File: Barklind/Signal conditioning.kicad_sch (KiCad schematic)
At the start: 37 parts, among them J1 Conn_01x07_Socket, J10 Conn_01x04_Pin, J11 Conn_01x04_Pin, J12 Conn_01x04_Pin, J13 Conn_01x04_Pin, J14 Conn_01x04_Pin, J15 Conn_01x03_Pin, J16 Conn_01x03_Pin, J17 Conn_01x03_Pin, J18 Conn_01x03_Pin, J19 Conn_01x03_Pin, J2 Conn_01x06_Socket, J20 Conn_01x03_Pin, J21 Conn_01x03_Socket, J22 Conn_01x03_Socket, J23 Conn_01x03_Socket, J24 Conn_01x03_Socket, J25 Conn_01x03_Socket, J26 Conn_01x03_Socket, J3 Conn_01x02_Socket, J4 Conn_01x03_Socket, J5 Conn_01x07_Pin, J6 Conn_01x06_Pin, J7 Conn_01x02_Pin, J8 Conn_01x03_Pin, J9 Conn_01x04_Pin, U7 74HCT04

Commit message: Restructured project, Changed kibot configurations into different files Changed github actions for the different jobs
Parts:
- J7: footprint TerminalBlock_Phoenix:TerminalBlock_Phoenix_PT-1,5-2-3.5-H_1x02_P3.50mm_Horizontal -> TerminalBlock_Phoenix:TerminalBlock_Phoenix_MKDS-3-2-5.08_1x02_P5.08mm_Horizontal
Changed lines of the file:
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@@
 			)
 		)
-		(property "Footprint" "TerminalBlock_Phoenix:TerminalBlock_Phoenix_PT-1,5-2-3.5-H_1x02_P3.50mm_Horizontal"
+		(property "Footprint" "TerminalBlock_Phoenix:TerminalBlock_Phoenix_MKDS-3-2-5.08_1x02_P5.08mm_Horizontal"
 			(at 86.36 157.48 0)
 			(effects

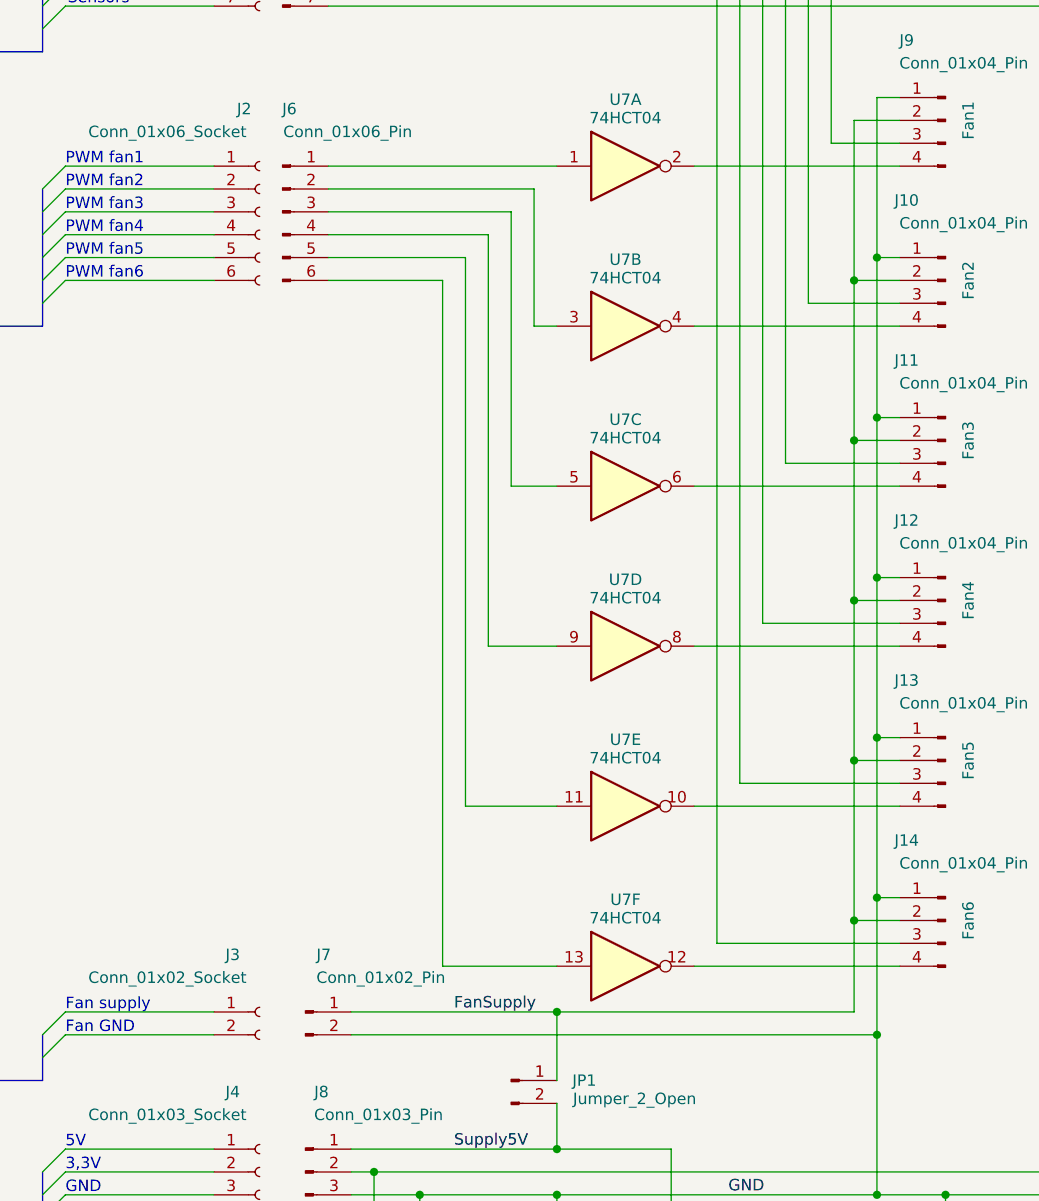
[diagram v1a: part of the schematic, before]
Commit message: Added pin header for pulling down unused inverter inputs
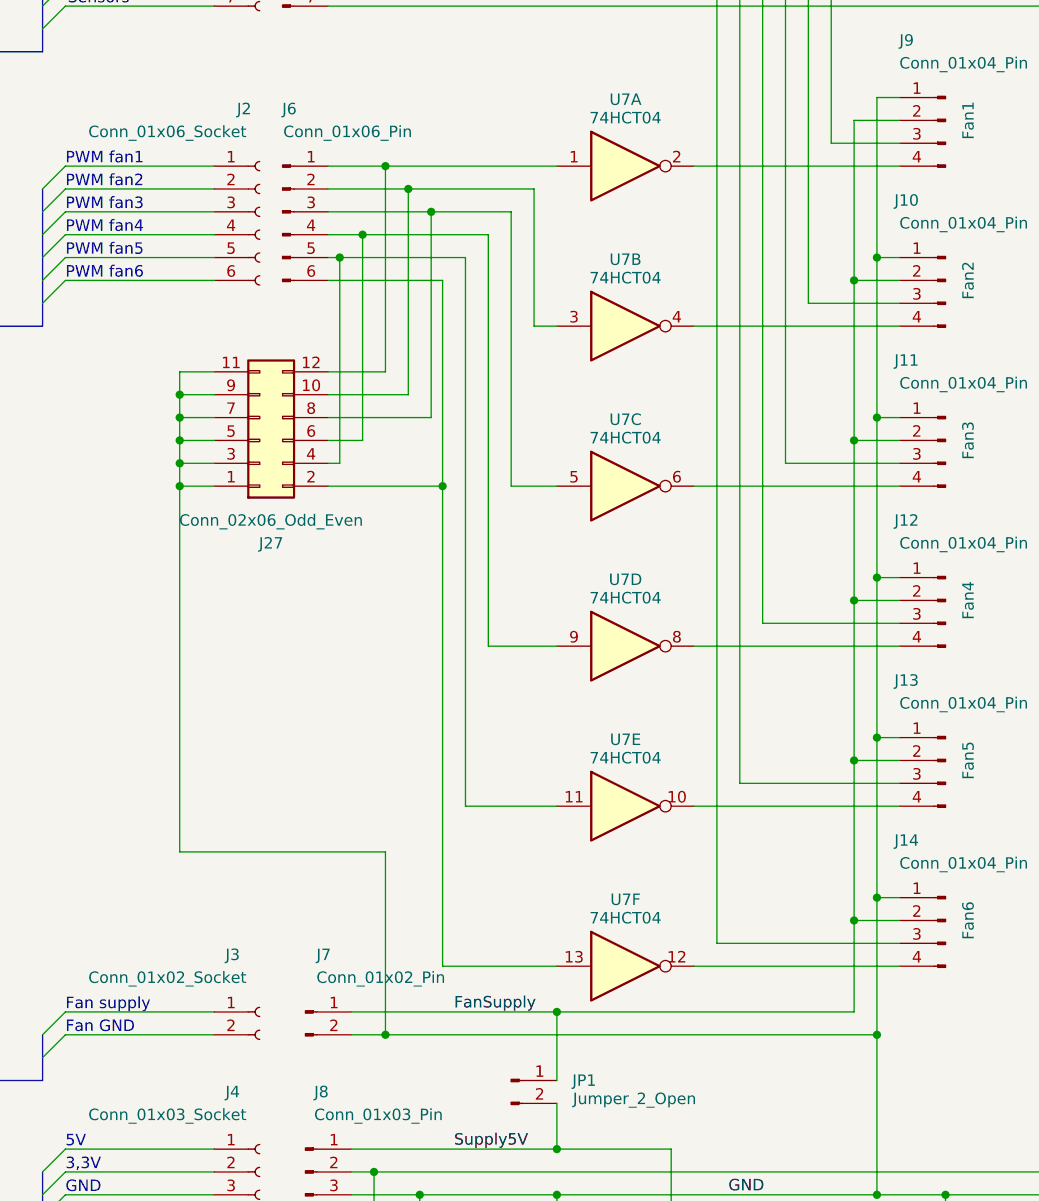
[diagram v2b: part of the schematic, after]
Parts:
- added J27: Conn_02x06_Odd_Even, Connector_PinHeader_1.27mm:PinHeader_2x06_P1.27mm_Vertical, symbol Connector_Generic:Conn_02x06_Odd_Even
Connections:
- net GND: now also J27.1 (Pin_1), J27.11 (Pin_11), J27.3 (Pin_3), J27.5 (Pin_5), J27.7 (Pin_7), J27.9 (Pin_9)
- net at J6.6 (Pin_6), U7.13: now also J27.2 (Pin_2)
- net at J6.2 (Pin_2), U7.3: now also J27.10 (Pin_10)
- net at J6.3 (Pin_3), U7.5: now also J27.8 (Pin_8)
- net at J6.5 (Pin_5), U7.11: now also J27.4 (Pin_4)
- net at J6.4 (Pin_4), U7.9: now also J27.6 (Pin_6)
- net at J6.1 (Pin_1), U7.1: now also J27.12 (Pin_12)

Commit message: Changed PCB to 4 layer and created manufacture files
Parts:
- J10, J11, J12, J13, J14, J9: footprint Connector_Molex:Molex_KK-254_AE-6410-04A_1x04_P2.54mm_Vertical -> Connector:FanPinHeader_1x04_P2.54mm_Vertical
- J7: footprint TerminalBlock_Phoenix:TerminalBlock_Phoenix_MKDS-3-2-5.08_1x02_P5.08mm_Horizontal -> Phoenix:PHOENIX_1705469
- R7: footprint Resistor_SMD:R_2010_5025Metric_Pad1.40x2.65mm_HandSolder -> Resistor_SMD:R_1206_3216Metric_Pad1.30x1.75mm_HandSolder
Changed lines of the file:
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@@
 	(label "GND"
 		(at 133.35 177.8 0)
+		(fields_autoplaced yes)
 		(effects
 			(font
@@
 	(label "FanSupply"
 		(at 102.87 157.48 0)
+		(fields_autoplaced yes)
 		(effects
 			(font
@@
 	(label "Supply5V"
 		(at 102.87 172.72 0)
+		(fields_autoplaced yes)
 		(effects
 			(font
@@
 		(shape output)
 		(at 228.6 119.38 0)
+		(fields_autoplaced yes)
 		(effects
 			(font
@@
 		(shape output)
 		(at 228.6 101.6 0)
+		(fields_autoplaced yes)
 		(effects
 			(font
@@
 		(shape input)
 		(at 50.8 50.8 180)
+		(fields_autoplaced yes)
 		(effects
 			(font
@@
 		(shape output)
 		(at 228.6 66.04 0)
+		(fields_autoplaced yes)
 		(effects
 			(font
@@
 		(shape output)
 		(at 228.6 137.16 0)
+		(fields_autoplaced yes)
 		(effects
 			(font
@@
 		(shape output)
 		(at 228.6 154.94 0)
+		(fields_autoplaced yes)
 		(effects
 			(font
@@
 		(shape input)
 		(at 50.8 182.88 180)
+		(fields_autoplaced yes)
 		(effects
 			(font
@@
 		(shape output)
 		(at 228.6 83.82 0)
+		(fields_autoplaced yes)
 		(effects
 			(font
@@
 		(shape output)
 		(at 50.8 81.28 180)
+		(fields_autoplaced yes)
 		(effects
 			(font
@@
 		(shape input)
 		(at 50.8 165.1 180)
+		(fields_autoplaced yes)
 		(effects
 			(font
@@
 			)
 		)
-		(property "Footprint" "Connector_Molex:Molex_KK-254_AE-6410-04A_1x04_P2.54mm_Vertical"
+		(property "Footprint" "Connector:FanPinHeader_1x04_P2.54mm_Vertical"
 			(at 157.48 147.32 0)
 			(effects
@@
 			)
 		)
-		(property "Footprint" "Connector_Molex:Molex_KK-254_AE-6410-04A_1x04_P2.54mm_Vertical"
+		(property "Footprint" "Connector:FanPinHeader_1x04_P2.54mm_Vertical"
 			(at 157.48 76.2 0)
 			(effects
@@
 			)
 		)
-		(property "Footprint" "Resistor_SMD:R_2010_5025Metric_Pad1.40x2.65mm_HandSolder"
+		(property "Footprint" "Resistor_SMD:R_1206_3216Metric_Pad1.30x1.75mm_HandSolder"
 			(at 170.942 24.13 90)
 			(effects
@@
 			)
 		)
-		(property "Footprint" "Connector_Molex:Molex_KK-254_AE-6410-04A_1x04_P2.54mm_Vertical"
+		(property "Footprint" "Connector:FanPinHeader_1x04_P2.54mm_Vertical"
 			(at 157.48 129.54 0)
 			(effects
@@
 			)
 		)
-		(property "Footprint" "Connector_Molex:Molex_KK-254_AE-6410-04A_1x04_P2.54mm_Vertical"
+		(property "Footprint" "Connector:FanPinHeader_1x04_P2.54mm_Vertical"
 			(at 157.48 93.98 0)
 			(effects
@@
 			)
 		)
-		(property "Footprint" "TerminalBlock_Phoenix:TerminalBlock_Phoenix_MKDS-3-2-5.08_1x02_P5.08mm_Horizontal"
+		(property "Footprint" "Phoenix:PHOENIX_1705469"
 			(at 86.36 157.48 0)
 			(effects
@@
 			)
 		)
-		(property "Footprint" "Connector_Molex:Molex_KK-254_AE-6410-04A_1x04_P2.54mm_Vertical"
+		(property "Footprint" "Connector:FanPinHeader_1x04_P2.54mm_Vertical"
 			(at 157.48 111.76 0)
 			(effects
@@
 			)
 		)
-		(property "Footprint" "Connector_Molex:Molex_KK-254_AE-6410-04A_1x04_P2.54mm_Vertical"
+		(property "Footprint" "Connector:FanPinHeader_1x04_P2.54mm_Vertical"
 			(at 157.48 58.42 0)
 			(effects
